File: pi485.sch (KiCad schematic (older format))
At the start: 20 parts, among them J1 RS485, P1 Rasperry Pi, P2 PWR, P3 Term, Q1 NPN, U1 NE555, U2 MAX485

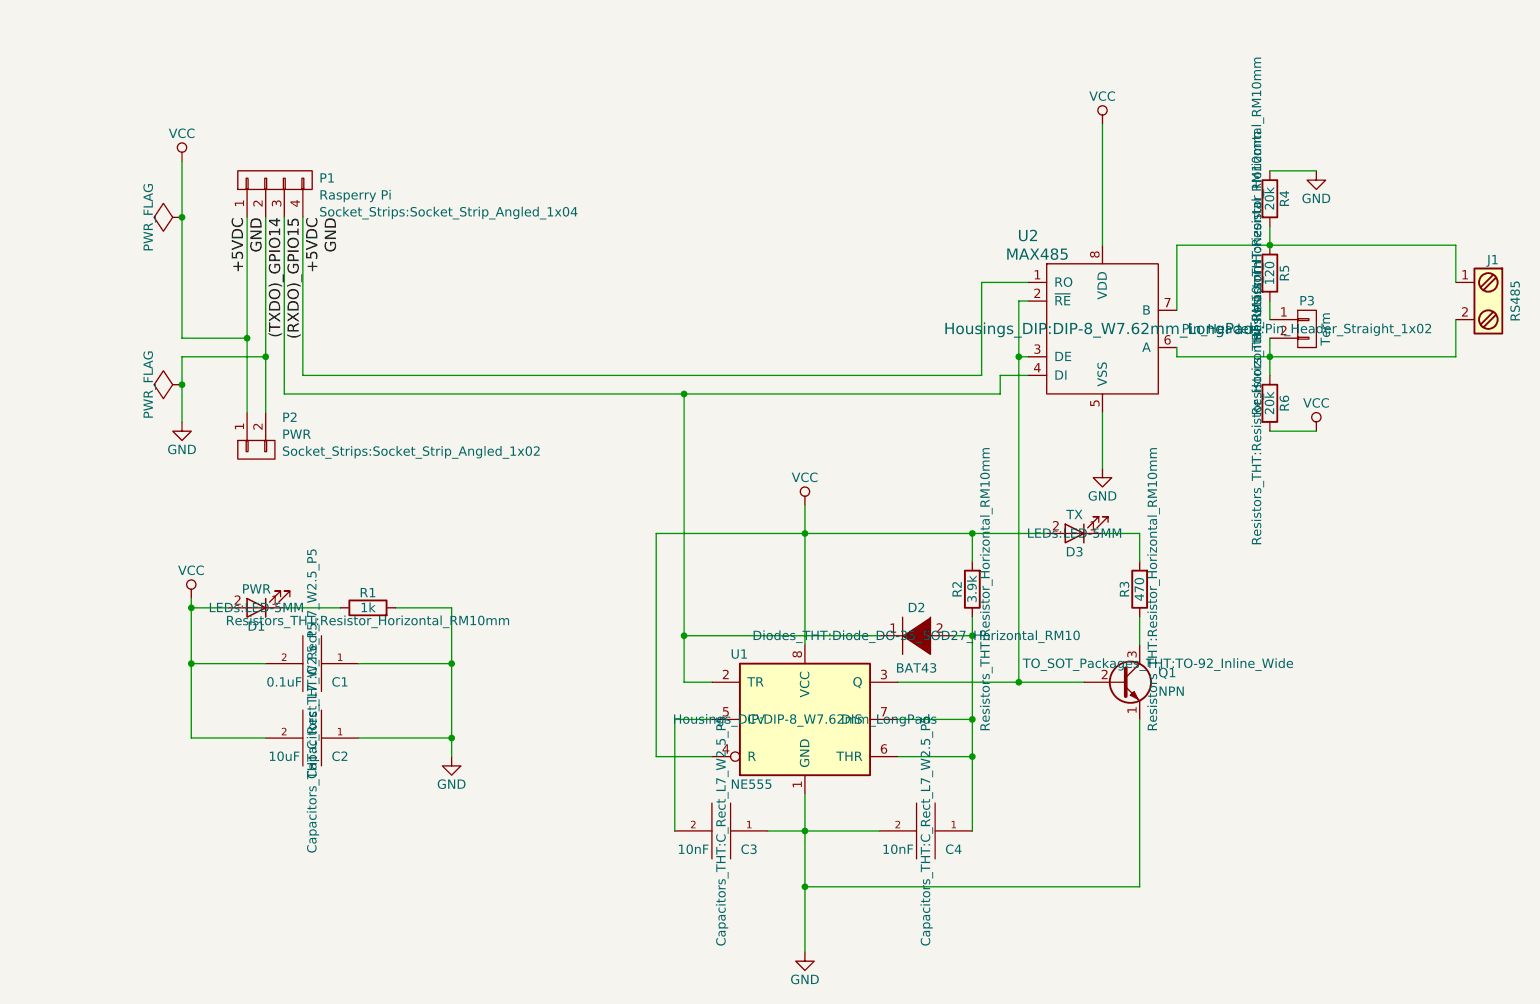
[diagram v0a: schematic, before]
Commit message: Made a bunch of changes...
New board size (70mm x 53mm) single layer, better layout.
Replace silicon diode with saturated NPN, added NPN tirggered TX / RX LEDs.
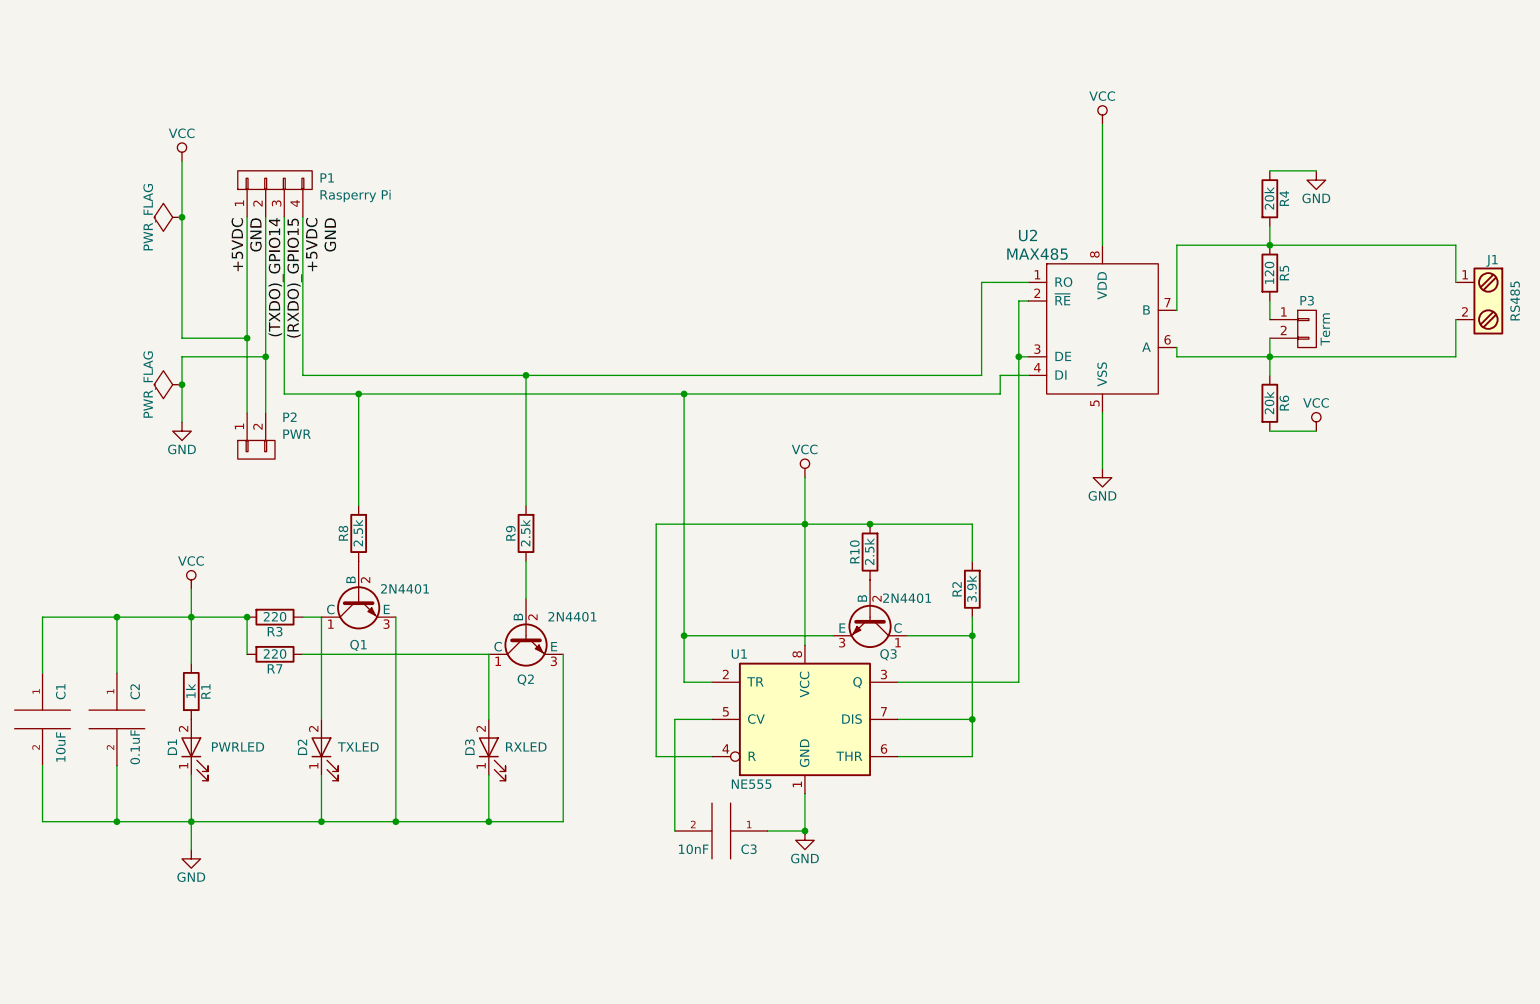
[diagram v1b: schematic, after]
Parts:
- removed C4: 10nF, Capacitors_THT:C_Rect_L7_W2.5_P5, symbol CAP
- removed D2: BAT43, Diodes_THT:Diode_DO-35_SOD27_Horizontal_RM10, symbol DIODE
- removed Q1: NPN, TO_SOT_Packages_THT:TO-92_Inline_Wide, symbol Q_NPN_EBC
- added D2: TXLED, LEDs:LED-5MM, symbol LED
- added Q1, Q2, Q3: 2N4401, TO_SOT_Packages_THT:TO-92_Inline_Narrow_Oval, symbol BC413
- added R10, R8, R9: 2.5k, Resistors_THT:Resistor_Horizontal_RM10mm, symbol R
- added R7: 220, Resistors_THT:Resistor_Horizontal_RM10mm, symbol R
- C1: value 0.1uF -> 10uF
- C2: value 10uF -> 0.1uF
- D1: value PWR -> PWRLED
- D3: value TX -> RXLED
- R3: value 470 -> 220
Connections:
- net (RXDO)_GPIO15: now also R9.2
- net (TXDO)_GPIO14: now also Q3.3 (E), R8.2
- net GND: now also C1.2, C2.2, D1.1 (K), D3.1 (K), D2.1 (K), Q1.3 (E), Q2.3 (E); no longer C1.1, C2.1, R1.2
- net VCC: now also C1.1, C2.1, R1.1, R3.2, R10.2, R7.2; no longer C1.2, C2.2, D1.2 (A), D3.2 (A)
- net at R2.1, U1.6 (THR), U1.7 (DIS): now also Q3.1 (C)
- net at R3.1: now also D2.2 (A), Q1.1 (C)
- new net: D1.2 (A), R1.2
- new net: Q3.2 (B), R10.1
- new net: Q1.2 (B), R8.1
- new net: D3.2 (A), Q2.1 (C), R7.1
- new net: Q2.2 (B), R9.1
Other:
- moved on the sheet: D1, R1

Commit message: Updating...
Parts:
- Q1, Q2, Q3: value 2N4401 -> 2N2222; footprint TO_SOT_Packages_THT:TO-92_Inline_Narrow_Oval -> TO_SOT_Packages_THT:TO-92_Inline_Wide
- R1, R10, R2, R3, R4, R5, R6, R7, R9: footprint Resistors_THT:Resistor_Horizontal_RM10mm -> Resistors_THT:Resistor_Horizontal_RM7mm
- R8: footprint Resistors_THT:Resistor_Horizontal_RM10mm -> Resistors_THT:Resistor_Horizontal_RM15mm
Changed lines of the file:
@@
 encoding utf-8
 Sheet 1 1
-Title "Pi-485"
-Date "2017-1-6"
-Rev "1"
+Title "Pi485"
+Date "2017-01-12"
+Rev "1.0.0"
 Comp "Bryan Varner"
 Comment1 ""
 Comment2 ""
-Comment3 "Implements half-duplex RS485 with TX triggerd RE/DE control."
-Comment4 "Raspberry Pi UART to RS485"
+Comment3 "Implements half-duplex with TX latched RE/DE"
+Comment4 "Raspberry Pi / Arduino UART to RS485"
 $EndDescr
 $Comp
@@
 F 0 "R1" V 2280 4700 50  0000 C CNN
 F 1 "1k" V 2200 4700 50  0000 C CNN
-F 2 "Resistors_THT:Resistor_Horizontal_RM10mm" V 2350 4000 50  0001 C CNN
+F 2 "Resistors_THT:Resistor_Horizontal_RM7mm" V 2350 4000 50  0001 C CNN
 F 3 "" H 2200 4700 50  0000 C CNN
 	1    2200 4700
@@
 F 0 "R2" V 6480 4150 50  0000 C CNN
 F 1 "3.9k" V 6400 4150 50  0000 C CNN
-F 2 "Resistors_THT:Resistor_Horizontal_RM10mm" H 5500 4150 50  0001 C CNN
+F 2 "Resistors_THT:Resistor_Horizontal_RM7mm" H 5500 4150 50  0001 C CNN
 F 3 "" H 6400 4150 50  0000 C CNN
 	1    6400 4150
@@
 F 0 "R5" V 8080 2450 50  0000 C CNN
 F 1 "120" V 8000 2450 50  0000 C CNN
-F 2 "Resistors_THT:Resistor_Horizontal_RM10mm" H 8850 2650 50  0001 C CNN
+F 2 "Resistors_THT:Resistor_Horizontal_RM7mm" H 8850 2650 50  0001 C CNN
 F 3 "" H 8000 2450 50  0000 C CNN
 	1    8000 2450
@@
 F 0 "R4" V 8080 2050 50  0000 C CNN
 F 1 "20k" V 8000 2050 50  0000 C CNN
-F 2 "Resistors_THT:Resistor_Horizontal_RM10mm" H 8850 2300 50  0001 C CNN
+F 2 "Resistors_THT:Resistor_Horizontal_RM7mm" H 8850 2300 50  0001 C CNN
 F 3 "" H 8000 2050 50  0000 C CNN
 	1    8000 2050
@@
 F 0 "R6" V 8080 3150 50  0000 C CNN
 F 1 "20k" V 8000 3150 50  0000 C CNN
-F 2 "Resistors_THT:Resistor_Horizontal_RM10mm" H 8850 3300 50  0001 C CNN
+F 2 "Resistors_THT:Resistor_Horizontal_RM7mm" H 8850 3300 50  0001 C CNN
 F 3 "" H 8000 3150 50  0000 C CNN
 	1    8000 3150
@@
 F 0 "R10" V 5930 3950 50  0000 C CNN
 F 1 "2.5k" V 5850 3950 50  0000 C CNN
-F 2 "Resistors_THT:Resistor_Horizontal_RM10mm" H 4950 3950 50  0001 C CNN
+F 2 "Resistors_THT:Resistor_Horizontal_RM7mm" H 4950 3950 50  0001 C CNN
 F 3 "" H 5850 3950 50  0000 C CNN
 	1    5850 3950
@@
 P 5850 4300
 F 0 "Q3" V 6050 4400 50  0000 C CNN
-F 1 "2N4401" V 5750 4500 50  0000 C CNN
-F 2 "TO_SOT_Packages_THT:TO-92_Inline_Narrow_Oval" V 6268 4300 50  0001 C CIN
+F 1 "2N2222" V 5750 4500 50  0000 C CNN
+F 2 "TO_SOT_Packages_THT:TO-92_Inline_Wide" V 6268 4300 50  0001 C CIN
 F 3 "" H 5850 4300 50  0000 L CNN
 	1    5850 4300
@@
 P 3100 4200
 F 0 "Q1" V 3350 4200 50  0000 C CNN
-F 1 "2N4401" V 3050 3950 50  0000 C CNN
-F 2 "TO_SOT_Packages_THT:TO-92_Inline_Narrow_Oval" V 3518 4200 50  0001 C CIN
+F 1 "2N2222" V 3050 3950 50  0000 C CNN
+F 2 "TO_SOT_Packages_THT:TO-92_Inline_Wide" V 3518 4200 50  0001 C CIN
 F 3 "" H 3100 4200 50  0000 L CNN
 	1    3100 4200
@@
 P 4000 4400
 F 0 "Q2" V 4236 4400 50  0000 C CNN
-F 1 "2N4401" V 3900 4150 50  0000 C CNN
-F 2 "TO_SOT_Packages_THT:TO-92_Inline_Narrow_Oval" V 4418 4400 50  0001 C CIN
+F 1 "2N2222" V 3900 4150 50  0000 C CNN
+F 2 "TO_SOT_Packages_THT:TO-92_Inline_Wide" V 4418 4400 50  0001 C CIN
 F 3 "" H 4000 4400 50  0000 L CNN
 	1    4000 4400
@@
 F 0 "R7" V 2730 4500 50  0000 C CNN
 F 1 "220" V 2650 4500 50  0000 C CNN
-F 2 "Resistors_THT:Resistor_Horizontal_RM10mm" V 2800 3800 50  0001 C CNN
+F 2 "Resistors_THT:Resistor_Horizontal_RM7mm" V 2800 3800 50  0001 C CNN
 F 3 "" H 2650 4500 50  0000 C CNN
 	1    2650 4500
@@
 F 0 "R3" V 2730 4300 50  0000 C CNN
 F 1 "220" V 2650 4300 50  0000 C CNN
-F 2 "Resistors_THT:Resistor_Horizontal_RM10mm" V 2800 3600 50  0001 C CNN
+F 2 "Resistors_THT:Resistor_Horizontal_RM7mm" V 2800 3600 50  0001 C CNN
 F 3 "" H 2650 4300 50  0000 C CNN
 	1    2650 4300
@@
 F 0 "R8" V 3180 3850 50  0000 C CNN
 F 1 "2.5k" V 3100 3850 50  0000 C CNN
-F 2 "Resistors_THT:Resistor_Horizontal_RM10mm" V 3250 3150 50  0001 C CNN
+F 2 "Resistors_THT:Resistor_Horizontal_RM15mm" V 3250 3150 50  0001 C CNN
 F 3 "" H 3100 3850 50  0000 C CNN
 	1    3100 3850
@@
 F 0 "R9" V 4080 3850 50  0000 C CNN
 F 1 "2.5k" V 4000 3850 50  0000 C CNN
-F 2 "Resistors_THT:Resistor_Horizontal_RM10mm" V 4150 3150 50  0001 C CNN
+F 2 "Resistors_THT:Resistor_Horizontal_RM7mm" V 4150 3150 50  0001 C CNN
 F 3 "" H 4000 3850 50  0000 C CNN
 	1    4000 3850

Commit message: Switched A/B output on the RS485 screw terminal for pin 1 to be A, pin 2 to be B.
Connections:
- net at P3.2 (P2), R6.1, U2.6 (A): now also J1.1; no longer J1.2
- net at R4.2, R5.1, U2.7 (B): now also J1.2; no longer J1.1
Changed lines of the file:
@@
 Title "Pi485"
 Date "2017-01-12"
-Rev "1.0.0"
+Rev "1.0.1"
 Comp "Bryan Varner"
 Comment1 ""
@@
 L GND #PWR07
 U 1 1 586E98F0
-P 5500 5450
-F 0 "#PWR07" H 5500 5200 50  0001 C CNN
-F 1 "GND" H 5500 5300 50  0000 C CNN
-F 2 "" H 5500 5450 50  0000 C CNN
-F 3 "" H 5500 5450 50  0000 C CNN
-	1    5500 5450
+P 5500 5650
+F 0 "#PWR07" H 5500 5400 50  0001 C CNN
+F 1 "GND" H 5500 5500 50  0000 C CNN
+F 2 "" H 5500 5650 50  0000 C CNN
+F 3 "" H 5500 5650 50  0000 C CNN
+	1    5500 5650
 	1    0    0    -1
 $EndComp
@@
 F 3 "" H 9175 2600 50  0001 C CNN
 	1    9200 2600
-	-1   0    0    -1
+	-1   0    0    1
 $EndComp
 Text Label 2800 2150 3    60   ~ 0
@@
 	5300 5450 5500 5450
 Wire Wire Line
-	5500 5450 5500 5250
+	5500 5250 5500 5650
 Connection ~ 5500 5450
 Wire Wire Line
